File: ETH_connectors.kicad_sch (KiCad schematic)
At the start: 2 parts, among them J1 Bus_RJ45_5-2337992-8, J2 Bus_RJ45_5-2337992-8

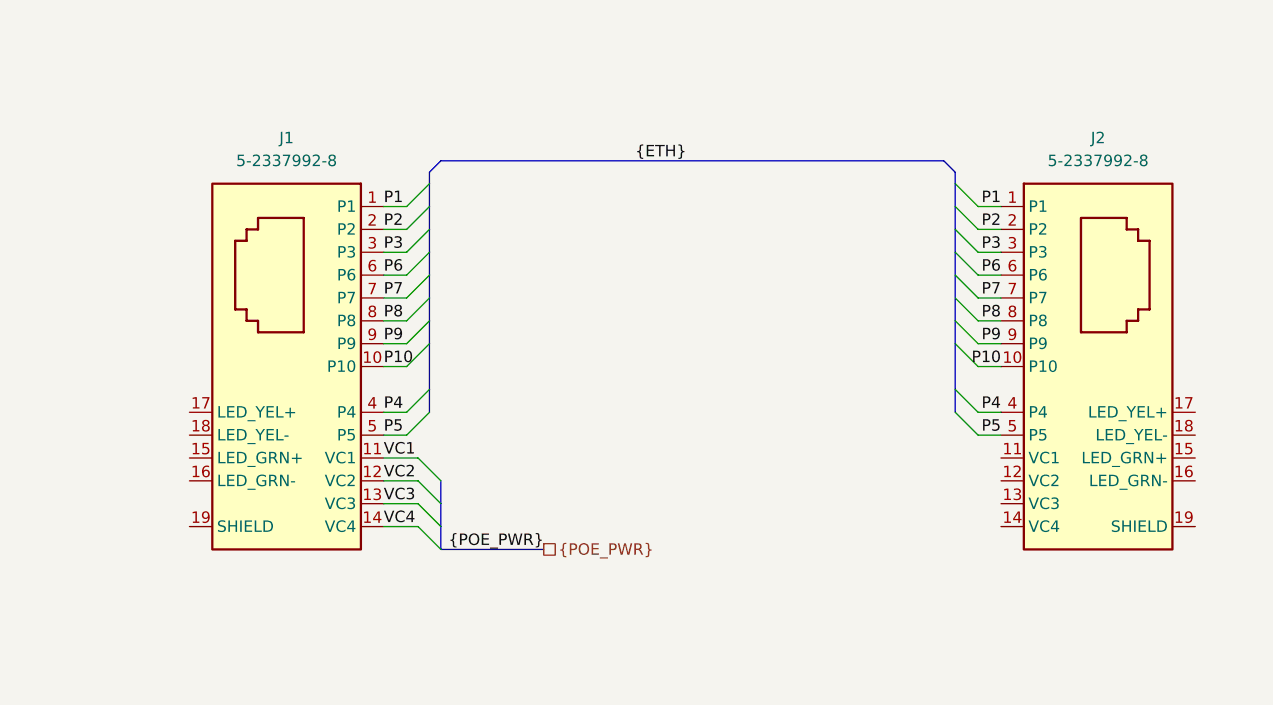
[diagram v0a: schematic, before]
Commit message: [#62623] Improve schematic, change 3V3 buck inductor, correct SPI, add testpoint
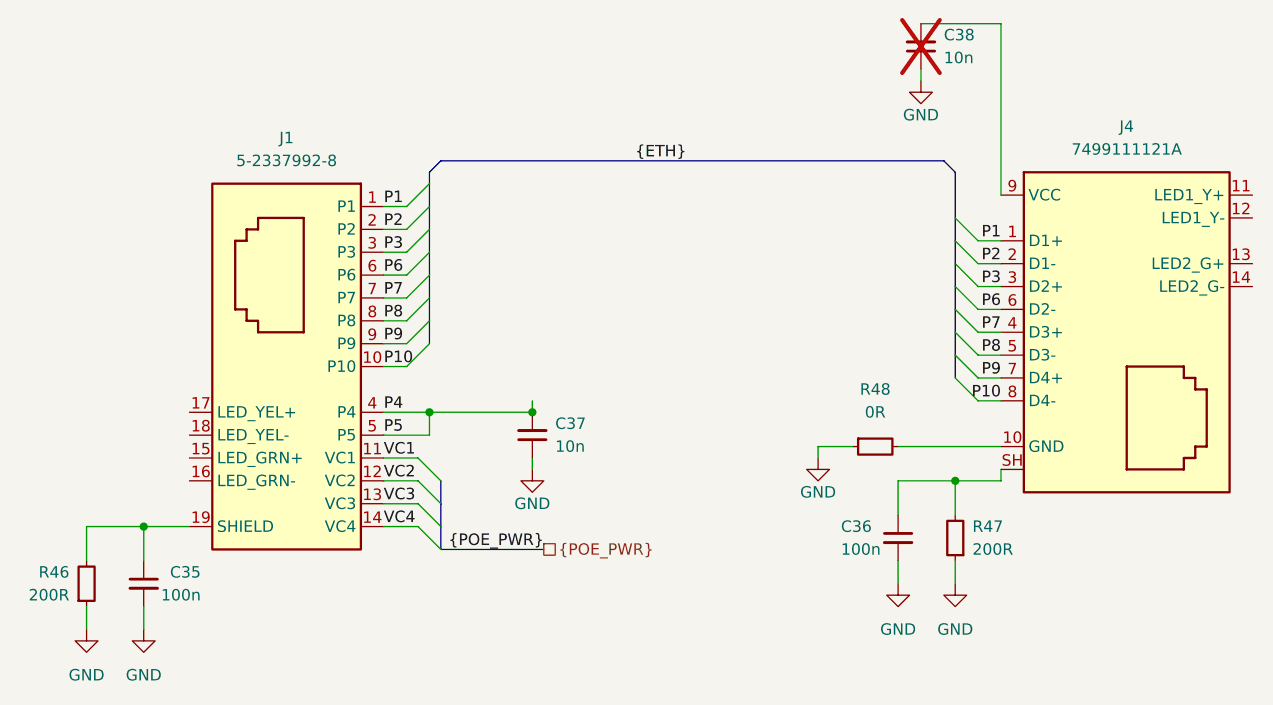
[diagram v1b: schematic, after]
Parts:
- removed J2: Bus_RJ45_5-2337992-8, antmicro-footprints:RJ45_X-2337992-8_Horizontal, symbol antmicroModularConnectorsJacksWithMagnetics:Bus_RJ45_5-2337992-8
- added C35, C36: C_100n_0402, antmicro-footprints:C_0402_1005Metric, symbol antmicroCapacitors0402:C_100n_0402
- added C37, C38: C_10n_0603, antmicro-footprints:C_0603_1608Metric, symbol antmicroCapacitors0603:C_10n_0603
- added J4: Bus_RJ45_7499111121A, antmicro-footprints:RJ45_7499111121A_Horizontal, symbol antmicroModularConnectorsJacksWithMagnetics:Bus_RJ45_7499111121A
- added R46, R47: R_200R_0402, antmicro-footprints:R_0402_1005Metric, symbol antmicroResistors0402:R_200R_0402
- added R48: R_0R_0402, antmicro-footprints:R_0402_1005Metric, symbol antmicroResistors0402:R_0R_0402
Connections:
- net P5 is gone; now on net P4: J1.5 (P5)
- net P1: now also J4.1 (D1+)
- net P10: now also J4.8 (D4-)
- net P2: now also J4.2 (D1-)
- net P3: now also J4.3 (D2+)
- net P4: now also C37.2
- net P6: now also J4.6 (D2-)
- net P7: now also J4.4 (D3+)
- net P8: now also J4.5 (D3-)
- net P9: now also J4.7 (D4+)
- net at J1.19 (SHIELD), J1.20 (SHIELD): now also C35.1, R46.2
- new net: J4.10 (GND), R48.2
- new net: C36.1, J4.SH, R47.2
- new net: C38.2, J4.9 (VCC)
- new net GND: C35.2, C36.2, C37.1, C38.1, R46.1, R47.1, R48.1
